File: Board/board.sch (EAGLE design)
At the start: 8 parts, among them IC1 L297, J1 +12V

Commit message: MCU + Kanda input
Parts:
- added C3, C4: 100nF, rcl:C-EU025-025X050
- added IC2: MEGA32-P, avr-7:MEGA32-P
- added KANDA: (no value), con-ml:ML10
- added OLED_SSD3306_CON: (no value), con-lsta:FE08-1
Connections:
- new net N$3: IC2.(MOSI)PB5, KANDA.1
- new net N$4: IC2.RESET, KANDA.5
- new net N$5: IC2.(SCK)PB7, KANDA.7
- new net N$6: IC2.(MISO)PB6, KANDA.9
- net GND: now also C3.2, C4.2, IC2.GND, KANDA.10, OLED_SSD3306_CON.2
- net VCC: now also C3.1, C4.1, IC2.AVCC, IC2.VCC, KANDA.2, OLED_SSD3306_CON.1
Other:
- moved on the sheet: F1, IC1

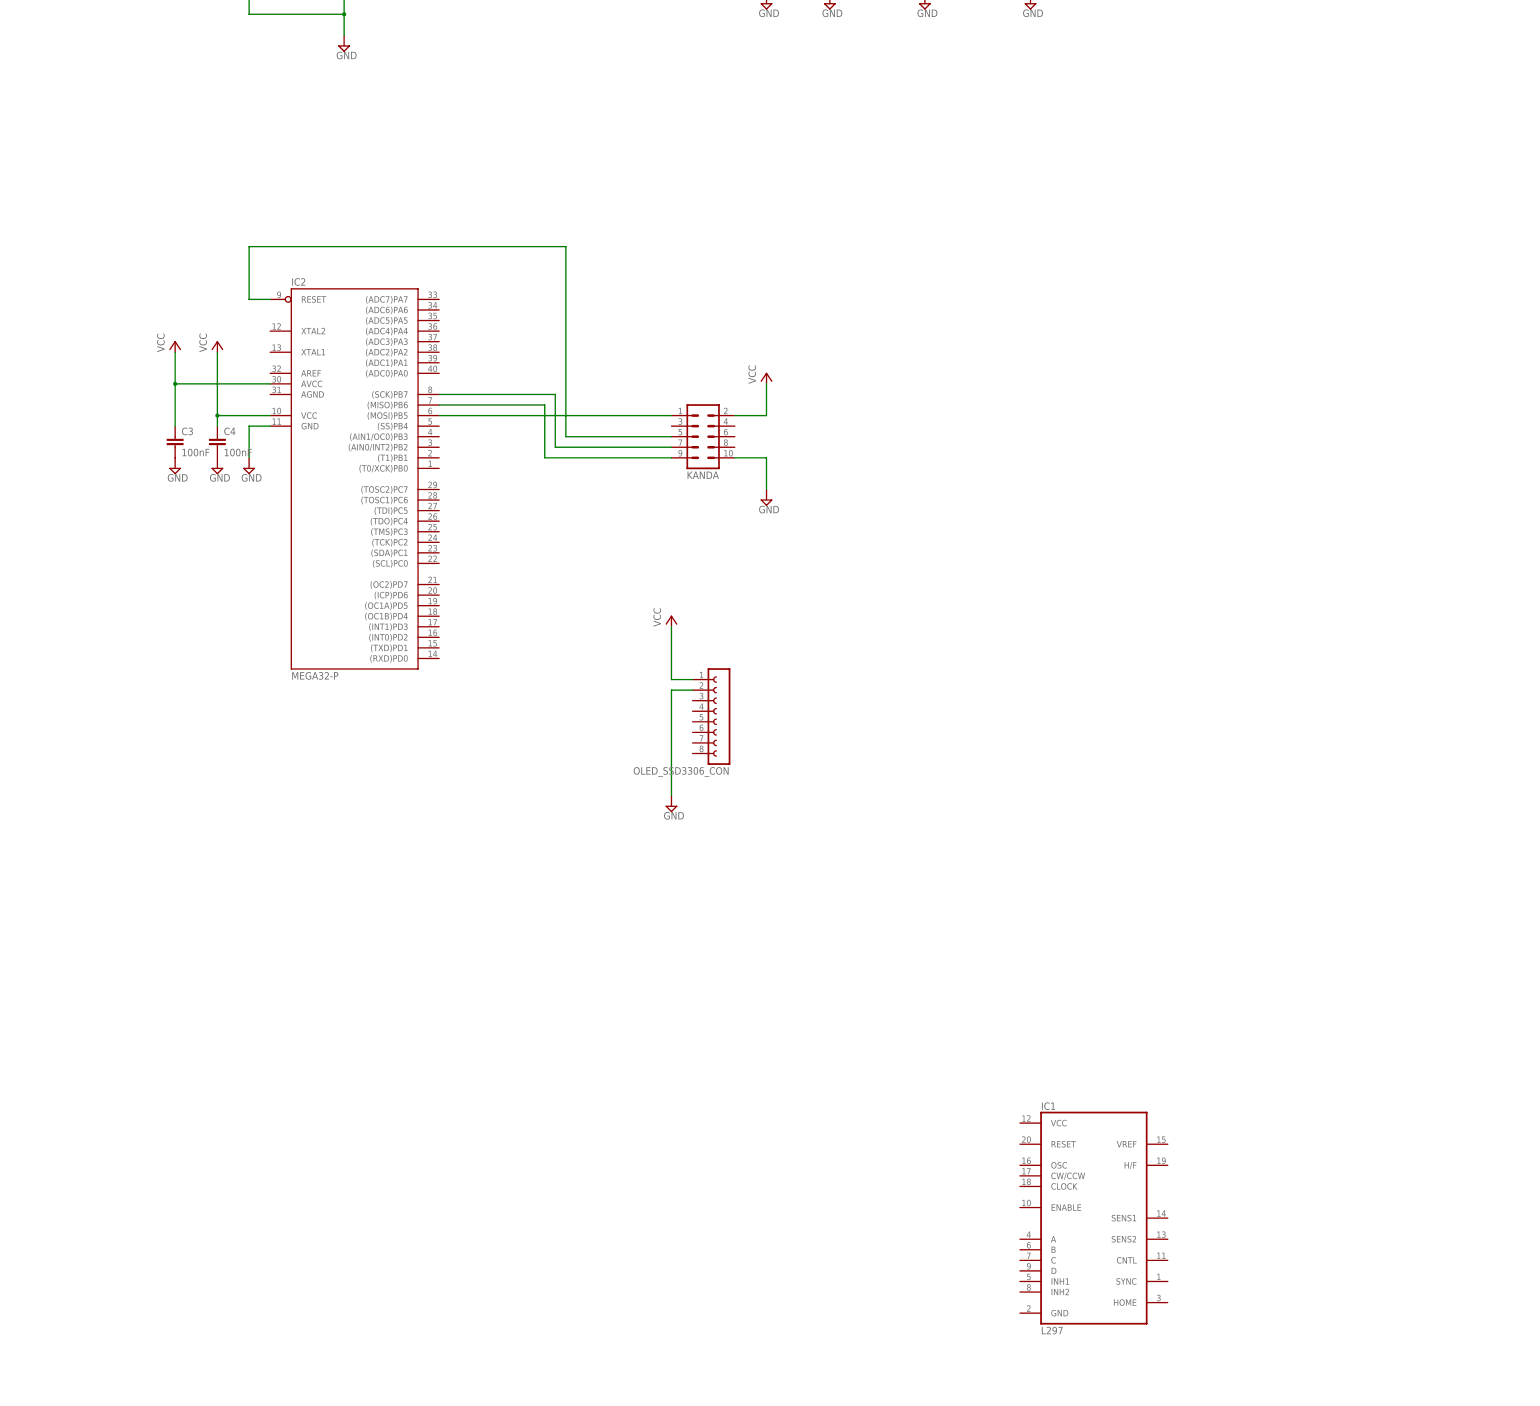
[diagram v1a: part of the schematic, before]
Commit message: Fan, water pump, and supply for motor drive eagle
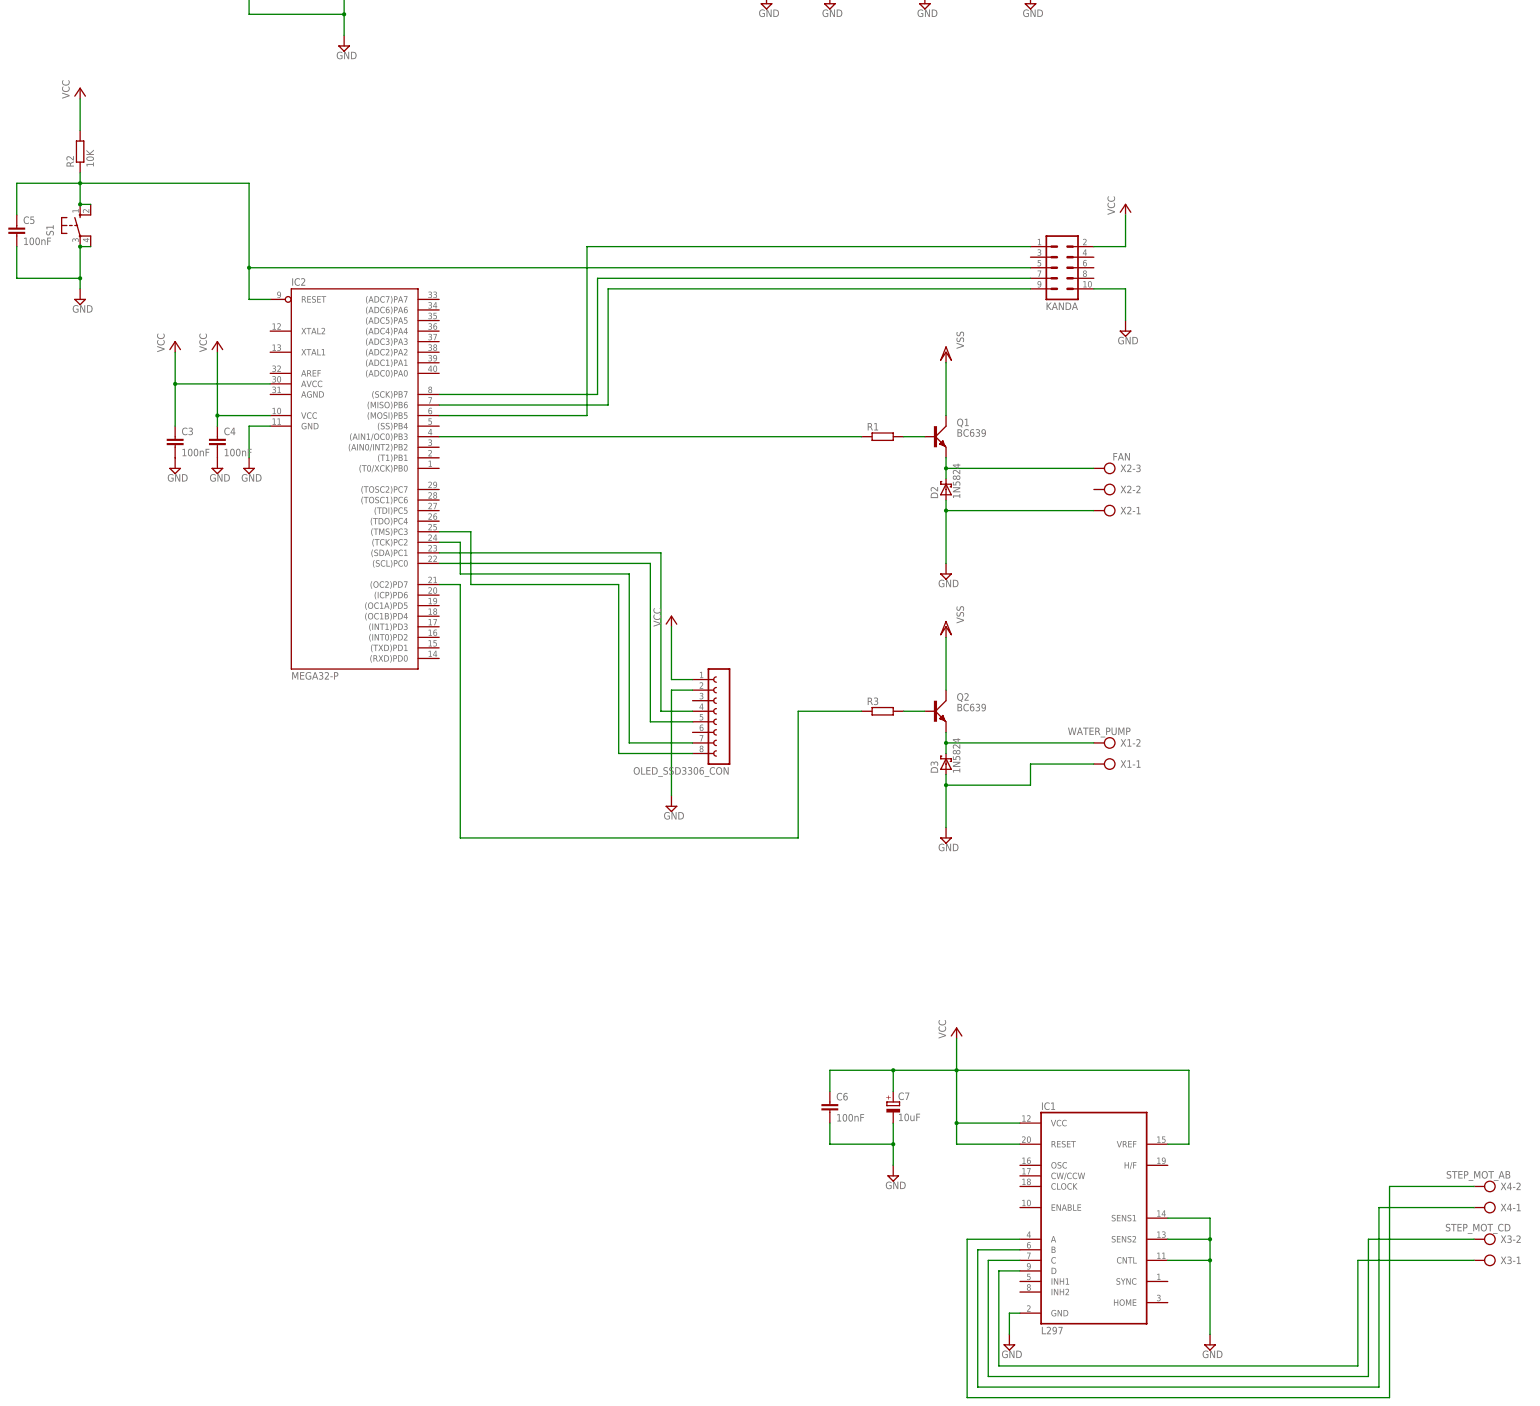
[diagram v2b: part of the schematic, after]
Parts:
- added C5, C6: 100nF, rcl:C-EU025-025X050
- added C7: 10uF, resistor:CPOL-EUE5-10.5
- added D2, D3: 1N5824, diode:1N5819-B
- added Q1, Q2: BC639, transistor-small-signal:BC639
- added R1, R3: (no value), rcl:R-EU_0207/12
- added R2: 10K, rcl:R-EU_0207/12
- added S1: (no value), switch-omron:10-XX
- added X1: WATER_PUMP, con-ptr500:AK500/2
- added X2: FAN, con-ptr500:AK500/3
- added X3: STEP_MOT_CD, con-ptr500:AK500/2
- added X4: STEP_MOT_AB, con-ptr500:AK500/2
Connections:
- removed net N$4 (its old number): IC2.RESET, KANDA.5
- new net N$10: C5.1, IC2.RESET, KANDA.5, R2.1, S1.S, S1.S1
- new net N$11: D3.C, Q2.E, X1-2.KL
- new net N$12: IC2.(OC2)PD7, R3.1
- new net N$13: IC1.D, X3-1.KL
- new net N$14: IC1.C, X3-2.KL
- new net N$15: IC1.B, X4-1.KL
- new net N$16: IC1.A, X4-2.KL
- new net N$5: D2.C, Q1.E, X2-3.KL
- new net N$7: Q2.B, R3.2
- new net N$8: Q1.B, R1.2
- new net N$9: IC2.(AIN1/OC0)PB3, R1.1
- new net OLED_RST: IC2.(TMS)PC3, OLED_SSD3306_CON.8
- new net OLED_SA: IC2.(TCK)PC2, OLED_SSD3306_CON.7
- new net SCL: IC2.(SCL)PC0, OLED_SSD3306_CON.5
- new net SDA: IC2.(SDA)PC1, OLED_SSD3306_CON.4
- net GND: now also C5.2, C6.2, C7.-, D2.A, D3.A, IC1.CNTL, IC1.GND, IC1.SENS1, IC1.SENS2, S1.P, S1.P1, X1-1.KL, X2-1.KL
- net VCC: now also C6.1, C7.+, IC1.RESET, IC1.VCC, IC1.VREF, R2.2
- net VSS: now also Q1.C, Q2.C
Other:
- moved on the sheet: KANDA

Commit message: L297 to uC
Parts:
- added CTRL_LED, LED1, LED2, LED3, LED4: (no value), led:LED3MM
- added D10, D11, D4, D5, D6, D7, D8, D9: 1N5819-B, diode:1N5819-B
- added Q3, Q4, Q5, Q6: BS170, transistor-small-signal:BS170
- added R10, R11, R4, R5, R6, R7, R8, R9: 47K, rcl:R-EU_0207/12
- added R12: 470R, rcl:R-EU_0207/12
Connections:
- new net N$17: IC1.CW/CCW, IC2.(ADC0)PA0
- new net N$18: IC1.CLOCK, IC2.(ADC1)PA1
- new net N$19: IC1.ENABLE, IC2.(ADC2)PA2
- new net N$20: IC1.H/F, IC2.(ADC3)PA3
- new net N$21: D4.A, D5.C, Q3.D, R5.1, X4-2.KL
- new net N$22: LED1.C, R5.2
- new net N$23: CTRL_LED.C, R12.2
- new net N$24: D6.A, D7.C, Q4.D, R7.1, X4-1.KL
- new net N$25: LED2.C, R7.2
- new net N$26: CTRL_LED.A, IC2.(AIN0/INT2)PB2
- new net N$27: D8.A, D9.C, Q5.D, R9.1, X3-2.KL
- new net N$28: LED3.C, R9.2
- new net N$29: Q6.G, R10.1
- new net N$30: D10.A, D11.C, Q6.D, R11.1, X3-1.KL
- new net N$31: LED4.C, R11.2
- new net N$32: Q3.G, R4.1
- net GND: now also D11.A, D5.A, D7.A, D9.A, Q3.S, Q4.S, Q5.S, Q6.S, R10.2, R12.1, R4.2, R6.2, R8.2
- net N$13: no longer X3-1.KL
- net N$14: now also Q4.G, R6.1; no longer X3-2.KL
- net N$15: now also Q5.G, R8.1; no longer X4-1.KL
- net N$16: no longer X4-2.KL
- net VCC: now also LED1.A, LED2.A, LED3.A, LED4.A
- net VSS: now also D10.C, D4.C, D6.C, D8.C
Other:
- moved on the sheet: X3-1, X3-2, X4-1, X4-2

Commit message: Signal leds to connectors
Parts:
- added FAN_LED, WP_LED: (no value), led:LED3MM
- added R13, R14: 470R, rcl:R-EU_0207/12
- R11, R5, R7, R9: value 47K -> 330R
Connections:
- new net N$33: FAN_LED.A, R13.1
- new net N$34: R14.1, WP_LED.A
- net N$11: now also R14.2
- net N$5: now also R13.2
- net VCC: now also FAN_LED.C, WP_LED.C
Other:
- moved on the sheet: D2, D3, X1-1, X1-2, X2-1, X2-2, X2-3

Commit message: mcp9808
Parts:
- added C8: 100nF, rcl:C-EU025-025X050
- added U1: MCP9808MSOP, MCP9808:MCP9808MSOP
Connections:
- removed net OLED_RST: IC2.(TMS)PC3, OLED_SSD3306_CON.8
- removed net OLED_SA: IC2.(TCK)PC2, OLED_SSD3306_CON.7
- removed net SCL: IC2.(SCL)PC0, OLED_SSD3306_CON.5
- removed net SDA: IC2.(SDA)PC1, OLED_SSD3306_CON.4
- new net N$35: IC2.(SDA)PC1, OLED_SSD3306_CON.4, U1.SDA
- new net N$36: IC2.(SCL)PC0, OLED_SSD3306_CON.5, U1.SCL
- new net N$37: IC2.(TCK)PC2, OLED_SSD3306_CON.6
- new net N$38: IC2.(TMS)PC3, OLED_SSD3306_CON.7
- new net N$39: IC2.(TDO)PC4, OLED_SSD3306_CON.8
- net GND: now also C8.2, U1.A0, U1.A1, U1.A2, U1.GND
- net VCC: now also C8.1, U1.VDD
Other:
- moved on the sheet: OLED_SSD3306_CON

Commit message: stepper motor l298
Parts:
- removed D11: 1N5819-B, diode:1N5819-B
- removed LED1, LED2, LED3, LED4: (no value), led:LED3MM
- removed Q2: BC639, transistor-small-signal:BC639
- removed Q4, Q5, Q6: BS170, transistor-small-signal:BS170
- removed R10, R6, R8: 47K, rcl:R-EU_0207/12
- removed R11, R9: 330R, rcl:R-EU_0207/12
- removed R13, R14: 470R, rcl:R-EU_0207/12
- removed R3: (no value), rcl:R-EU_0207/12
- removed X3: STEP_MOT_CD, con-ptr500:AK500/2
- removed X4: STEP_MOT_AB, con-ptr500:AK500/2
- added IC3: L298, st-microelectronics:L298
- added X5: STEP_MOT_CD, con-ptr500:AK500/2
- added X6: STEP_MOT_AB, con-ptr500:AK500/2
- D10, D4, D5, D6, D7, D8, D9: value 1N5819-B -> 1N5824
- Q3: value BS170 -> BC639; device transistor-small-signal:BS170 -> transistor-small-signal:BC639
- R4: value 47K -> 470R
- R5: value 330R -> (none)
- R7: value 330R -> 470R
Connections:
- removed net N$11: D3.C, Q2.E, R14.2, X1-2.KL
- removed net N$14: IC1.C, Q4.G, R6.1
- removed net N$22: LED1.C, R5.2
- removed net N$24: D6.A, D7.C, Q4.D, R7.1, X4-1.KL
- removed net N$25: LED2.C, R7.2
- removed net N$30: D10.A, D11.C, Q6.D, R11.1, X3-1.KL
- removed net N$31: LED4.C, R11.2
- removed net N$32: Q3.G, R4.1
- removed net N$34: R14.1, WP_LED.A
- removed net N$5 (its old number): D2.C, Q1.E, R13.2, X2-3.KL
- removed net N$7: Q2.B, R3.2
- new net N$56: IC1.C, IC3.INPUT2
- new net N$58: IC1.B, IC3.INPUT3
- new net N$9: Q1.C, X2-1.KL
- new net VSS1: D10.C, D3.A, D4.A, D5.A, D6.A, D7.C, D8.C, D9.C, IC3.OUT1, IC3.OUT2, IC3.OUT3, IC3.OUT4, X5-1.KL, X5-2.KL, X6-1.KL, X6-2.KL
- net GND: now also D10.A, D8.A, FAN_LED.A, IC3.GND, IC3.SEN_A, IC3.SEN_B, Q1.E, Q3.E, R4.1, R7.1, WP_LED.A; no longer D11.A, D2.A, D3.A, D5.A, Q3.S, Q4.S, Q5.S, Q6.S, R10.2, R4.2, R6.2, R8.2, X1-1.KL, X2-1.KL
- net N$12: now also R5.1; no longer R3.1
- net N$13: now also IC3.INPUT1
- net N$15: now also IC1.INH1, IC3.ENABLE_A; no longer IC1.B, Q5.G, R8.1
- net N$16: now also IC3.INPUT4
- net N$21: now also IC1.INH2, IC3.ENABLE_B; no longer D4.A, D5.C, Q3.D, R5.1, X4-2.KL
- net N$27: now also FAN_LED.C, R4.2; no longer D8.A, D9.C, Q5.D, R9.1, X3-2.KL
- net N$28: now also Q3.B, R5.2; no longer LED3.C, R9.2
- net N$29: now also D2.A, Q3.C, X1-1.KL; no longer Q6.G, R10.1
- net N$33: now also R7.2, WP_LED.C; no longer FAN_LED.A, R13.1
- net VCC: now also IC3.VCC; no longer FAN_LED.C, LED1.A, LED2.A, LED3.A, LED4.A, WP_LED.C
- net VSS: now also D2.C, D3.C, D5.C, IC3.VS, X1-2.KL, X2-3.KL; no longer D10.C, D8.C, Q1.C, Q2.C
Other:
- moved on the sheet: CTRL_LED, D10, D2, D3, D4, D5, D6, D7, D8, D9, FAN_LED, KANDA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

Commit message: added filter for vss l298
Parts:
- added C10: 22uF, resistor:CPOL-EUE5-10.5
- added C9: 100nF, rcl:C-EU025-025X050
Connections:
- net GND: now also C10.-, C9.2
- net VSS: now also C10.+, C9.1
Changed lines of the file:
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@@
 <setting verticaltext="up"/>
 </settings>
-<grid distance="0.1" unitdist="inch" unit="inch" style="lines" multiple="1" display="no" altdistance="0.01" altunitdist="inch" altunit="inch"/>
+<grid distance="0.1" unitdist="inch" unit="inch" style="dots" multiple="1" display="yes" altdistance="0.01" altunitdist="inch" altunit="inch"/>
 <layers>
 <layer number="1" name="Top" color="4" fill="1" visible="no" active="no"/>
@@
 <part name="D9" library="diode" deviceset="1N581*" device="" technology="9-B" value="1N5824"/>
 <part name="D10" library="diode" deviceset="1N581*" device="" technology="9-B" value="1N5824"/>
+<part name="SUPPLY28" library="supply2" deviceset="GND" device=""/>
+<part name="C9" library="rcl" deviceset="C-EU" device="025-025X050" value="100nF"/>
+<part name="C10" library="resistor" deviceset="CPOL-EU" device="E5-10.5" value="22uF"/>
 </parts>
 <sheets>
@@
 <instance part="SUPPLY17" gate="GND" x="215.9" y="-198.12"/>
 <instance part="SUPPLY18" gate="GND" x="256.54" y="-198.12"/>
-<instance part="VSS5" gate="G$1" x="256.54" y="-124.46" rot="R180"/>
+<instance part="VSS5" gate="G$1" x="256.54" y="-104.14" rot="R180"/>
 <instance part="X5" gate="-1" x="330.2" y="-172.72" rot="R180"/>
 <instance part="X5" gate="-2" x="330.2" y="-167.64" rot="R180"/>
@@
 <instance part="D9" gate="G$1" x="284.48" y="-187.96" rot="R90"/>
 <instance part="D10" gate="G$1" x="294.64" y="-187.96" rot="R90"/>
+<instance part="SUPPLY28" gate="GND" x="241.3" y="-137.16"/>
+<instance part="C9" gate="G$1" x="226.06" y="-119.38"/>
+<instance part="C10" gate="G$1" x="241.3" y="-119.38"/>
 </instances>
 <busses>
@@
 <segment>
 <pinref part="VSS5" gate="G$1" pin="VSS"/>
-<wire x1="256.54" y1="-127" x2="256.54" y2="-129.54" width="0.1524" layer="91"/>
+<wire x1="256.54" y1="-106.68" x2="256.54" y2="-111.76" width="0.1524" layer="91"/>
 <pinref part="IC3" gate="L298" pin="VS"/>
+<wire x1="256.54" y1="-111.76" x2="256.54" y2="-129.54" width="0.1524" layer="91"/>
 <wire x1="256.54" y1="-129.54" x2="256.54" y2="-152.4" width="0.1524" layer="91"/>
 <wire x1="256.54" y1="-152.4" x2="251.46" y2="-152.4" width="0.1524" layer="91"/>
@@
 <pinref part="D6" gate="G$1" pin="C"/>
 <wire x1="294.64" y1="-129.54" x2="294.64" y2="-144.78" width="0.1524" layer="91"/>
+<pinref part="C9" gate="G$1" pin="1"/>
+<wire x1="226.06" y1="-116.84" x2="226.06" y2="-111.76" width="0.1524" layer="91"/>
+<wire x1="226.06" y1="-111.76" x2="241.3" y2="-111.76" width="0.1524" layer="91"/>
+<pinref part="C10" gate="G$1" pin="+"/>
+<wire x1="241.3" y1="-111.76" x2="241.3" y2="-116.84" width="0.1524" layer="91"/>
+<wire x1="241.3" y1="-111.76" x2="256.54" y2="-111.76" width="0.1524" layer="91"/>
+<junction x="241.3" y="-111.76"/>
+<junction x="256.54" y="-111.76"/>
 </segment>
 <segment>
@@
 <wire x1="294.64" y1="-190.5" x2="294.64" y2="-195.58" width="0.1524" layer="91"/>
 </segment>
+<segment>
+<pinref part="SUPPLY28" gate="GND" pin="GND"/>
+<wire x1="241.3" y1="-124.46" x2="241.3" y2="-129.54" width="0.1524" layer="91"/>
+<pinref part="C10" gate="G$1" pin="-"/>
+<pinref part="C9" gate="G$1" pin="2"/>
+<wire x1="241.3" y1="-129.54" x2="241.3" y2="-134.62" width="0.1524" layer="91"/>
+<wire x1="226.06" y1="-124.46" x2="226.06" y2="-129.54" width="0.1524" layer="91"/>
+<wire x1="226.06" y1="-129.54" x2="241.3" y2="-129.54" width="0.1524" layer="91"/>
+<junction x="241.3" y="-129.54"/>
+</segment>
 </net>

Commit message: Added pcb design #1
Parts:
- added C11: 100nF, rcl:C-EU025-025X050
- added R3: 470R, rcl:R-EU_0207/12
- added VSS_LED: (no value), led:LED3MM
- CTRL_LED, FAN_LED, WP_LED: device led:LED3MM -> led:LED5MM
- R12: value 470R -> 330R
- X5: value STEP_MOT_CD -> SM_CD
- X6: value STEP_MOT_AB -> SM_AB
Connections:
- removed net N$27: FAN_LED.C, R4.2
- removed net N$33: R7.2, WP_LED.C
- new net N$11: IC2.(TDI)PC5, R12.2
- new net N$14: CTRL_LED.A, R12.1
- new net N$22: R7.1, WP_LED.A
- new net N$24: D5.A, D9.C, IC3.OUT3, X5-2.KL
- new net N$7: R3.2, VSS_LED.C
- net GND: now also C11.2, CTRL_LED.C, FAN_LED.C, R3.1, R4.2, R7.2, WP_LED.C; no longer FAN_LED.A, R12.1, R4.1, R7.1, WP_LED.A
- net N$23: now also FAN_LED.A, R4.1; no longer CTRL_LED.C, R12.2
- net N$26: no longer CTRL_LED.A
- net VCC: now also C11.1
- net VSS: now also VSS_LED.A
- net VSS1: no longer D5.A, D9.C, IC3.OUT3, X5-2.KL
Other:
- moved on the sheet: CTRL_LED, FAN_LED, R12, R4, R7, WP_LED
